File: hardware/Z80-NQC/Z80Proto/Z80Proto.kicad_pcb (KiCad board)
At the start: 2 copper layers, 59.7 x 99.7 mm, 23 parts, among them J1 Conn_01x38, U1 Z80CPU, U2 HM62256, U3 28C256, U4 74HC14, U5 74LS32, Y1 Crystal

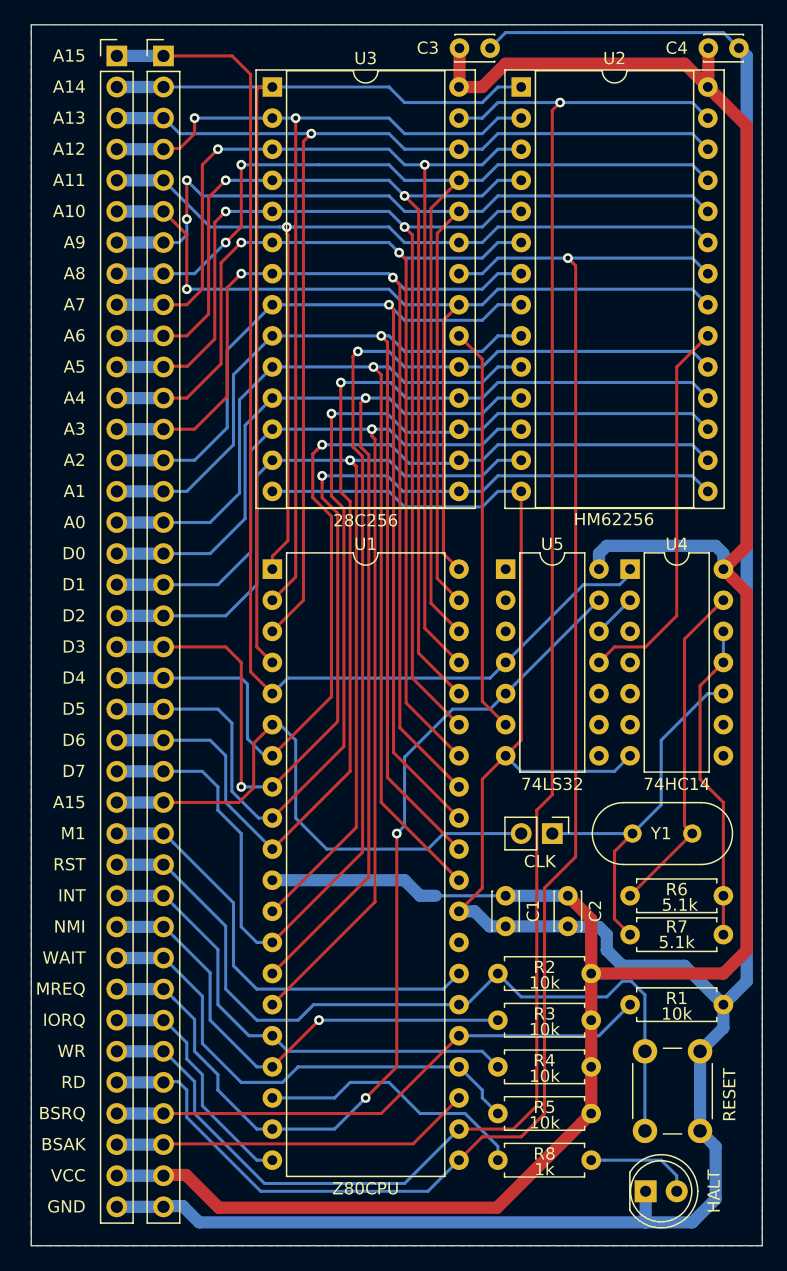
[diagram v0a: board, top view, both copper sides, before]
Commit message: Upgraded project formats to kicad 6.0
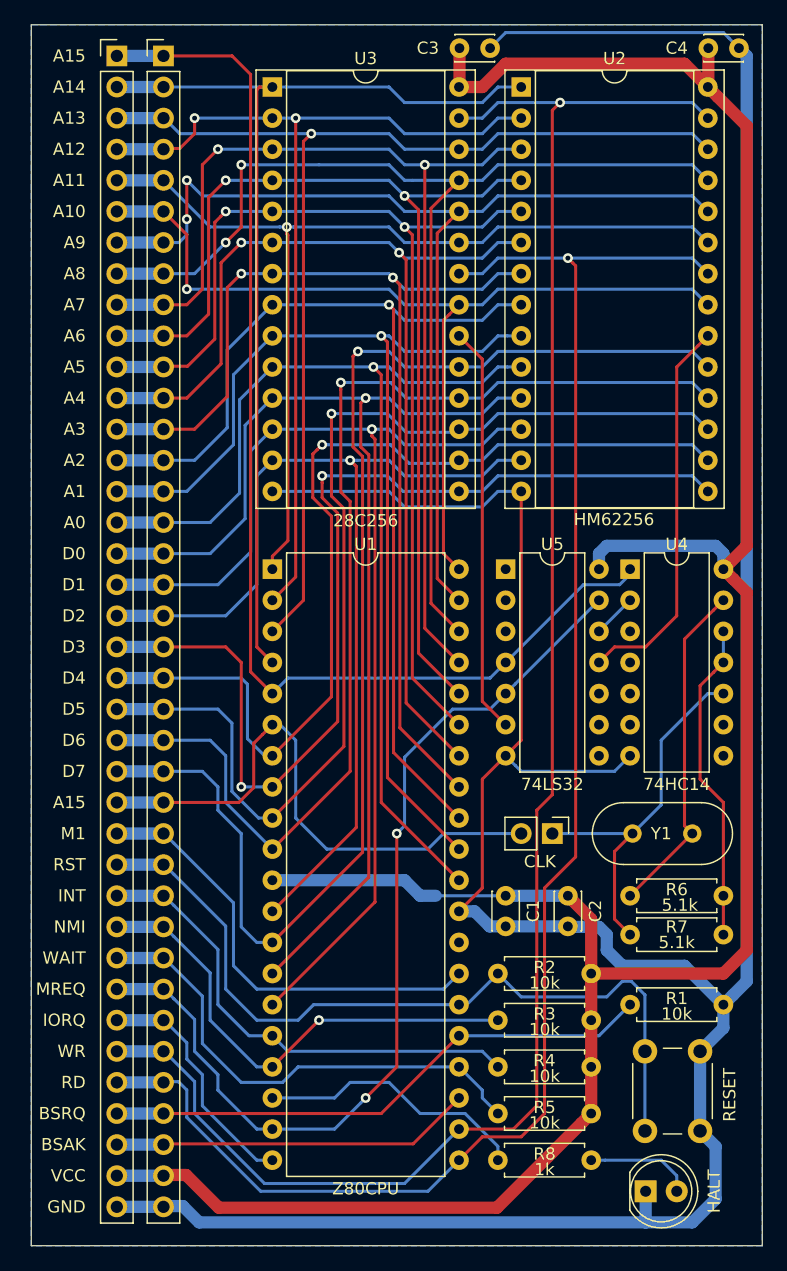
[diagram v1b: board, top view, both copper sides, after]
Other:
- net class Default removed
